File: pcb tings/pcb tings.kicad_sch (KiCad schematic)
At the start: 2 parts

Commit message: Finally back to working on this
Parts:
- added C?: 1uF, symbol Device:C_Small
- added R? (x2): 22, symbol Device:R_Small
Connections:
- net GND: now also C?.2
- net at U?.3 (D-): now also R?.2
- net at U?.4 (D+): now also R?.2
- net at U?.6 (UCAP): now also C?.1
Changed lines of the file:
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@@
   (junction (at 55.88 50.8) (diameter 0) (color 0 0 0 0)
   )
+  (wire (pts (xy 35.56 83.82) (xy 43.18 83.82))
+    (stroke (width 0) (type default) (color 0 0 0 0))
+  )
+  (wire (pts (xy 29.21 86.36) (xy 43.18 86.36))
+    (stroke (width 0) (type default) (color 0 0 0 0))
+  )
+  (wire (pts (xy 20.32 83.82) (xy 30.48 83.82))
+    (stroke (width 0) (type default) (color 0 0 0 0))
+  )
+  (wire (pts (xy 20.32 86.36) (xy 24.13 86.36))
+    (stroke (width 0) (type default) (color 0 0 0 0))
+  )
   (wire (pts (xy 73.66 111.76) (xy 90.17 111.76))
     (stroke (width 0) (type default) (color 0 0 0 0))
@@
     (stroke (width 0) (type default) (color 0 0 0 0))
   )
+  (wire (pts (xy 29.21 91.44) (xy 43.18 91.44))
+    (stroke (width 0) (type default) (color 0 0 0 0))
+  )
   (wire (pts (xy 58.42 50.8) (xy 60.96 50.8))
+    (stroke (width 0) (type default) (color 0 0 0 0))
+  )
+  (wire (pts (xy 29.21 96.52) (xy 29.21 99.06))
     (stroke (width 0) (type default) (color 0 0 0 0))
   )
@@
     (pin "1")
   )
+  (symbol (lib_id "Device:R_Small") (at 26.67 86.36 90) (unit 1)
+    (in_bom yes) (on_board yes)
+    (property "Reference" "R?" (id 0) (at 26.67 81.28 90))
+    (property "Value" "22" (id 1) (at 26.67 83.82 90))
+    (property "Footprint" "" (id 2) (at 26.67 86.36 0)
+      (effects (font (size 1.27 1.27)) hide)
+    )
+    (property "Datasheet" "~" (id 3) (at 26.67 86.36 0)
+      (effects (font (size 1.27 1.27)) hide)
+    )
+    (pin "1")
+    (pin "2")
+  )
   (symbol (lib_id "power:+5V") (at 55.88 44.45 0) (unit 1)
     (in_bom yes) (on_board yes) (fields_autoplaced)
@@
     (pin "1")
   )
+  (symbol (lib_id "power:GND") (at 29.21 99.06 0) (unit 1)
+    (in_bom yes) (on_board yes) (fields_autoplaced)
+    (property "Reference" "#PWR?" (id 0) (at 29.21 105.41 0)
+      (effects (font (size 1.27 1.27)) hide)
+    )
+    (property "Value" "GND" (id 1) (at 29.21 104.14 0))
+    (property "Footprint" "" (id 2) (at 29.21 99.06 0)
+      (effects (font (size 1.27 1.27)) hide)
+    )
+    (property "Datasheet" "" (id 3) (at 29.21 99.06 0)
+      (effects (font (size 1.27 1.27)) hide)
+    )
+    (pin "1")
+  )
+  (symbol (lib_id "Device:R_Small") (at 33.02 83.82 90) (unit 1)
+    (in_bom yes) (on_board yes)
+    (property "Reference" "R?" (id 0) (at 34.29 78.74 90)
+      (effects (font (size 1.27 1.27)) (justify left))
+    )
+    (property "Value" "22" (id 1) (at 34.29 81.28 90)
+      (effects (font (size 1.27 1.27)) (justify left))
+    )
+    (property "Footprint" "" (id 2) (at 33.02 83.82 0)
+      (effects (font (size 1.27 1.27)) hide)
+    )
+    (property "Datasheet" "~" (id 3) (at 33.02 83.82 0)
+      (effects (font (size 1.27 1.27)) hide)
+    )
+    (pin "1")
+    (pin "2")
+  )
   (symbol (lib_id "MCU_Microchip_ATmega:ATmega32U4-A") (at 58.42 96.52 0) (unit 1)
-    (in_bom yes) (on_board yes) (fields_autoplaced)
-    (property "Reference" "U?" (id 0) (at 60.4394 142.24 0)
-      (effects (font (size 1.27 1.27)) (justify left))
-    )
-    (property "Value" "ATmega32U4-A" (id 1) (at 60.4394 144.78 0)
+    (in_bom yes) (on_board yes)
+    (property "Reference" "U?" (id 0) (at 59.69 143.51 0)
+      (effects (font (size 1.27 1.27)) (justify left))
+    )
+    (property "Value" "ATmega32U4-A" (id 1) (at 53.34 146.05 0)
       (effects (font (size 1.27 1.27)) (justify left))
     )
@@
   )
   (symbol (lib_id "power:GND") (at 48.26 142.24 0) (unit 1)
-    (in_bom yes) (on_board yes) (fields_autoplaced)
+    (in_bom yes) (on_board yes)
     (property "Reference" "#PWR?" (id 0) (at 48.26 148.59 0)
       (effects (font (size 1.27 1.27)) hide)
     )
-    (property "Value" "GND" (id 1) (at 48.26 147.32 0))
+    (property "Value" "GND" (id 1) (at 48.26 146.05 0))
     (property "Footprint" "" (id 2) (at 48.26 142.24 0)
       (effects (font (size 1.27 1.27)) hide)
@@
     (pin "2")
   )
+  (symbol (lib_id "Device:C_Small") (at 29.21 93.98 0) (unit 1)
+    (in_bom yes) (on_board yes) (fields_autoplaced)
+    (property "Reference" "C?" (id 0) (at 31.75 92.7162 0)
+      (effects (font (size 1.27 1.27)) (justify left))
+    )
+    (property "Value" "1uF" (id 1) (at 31.75 95.2562 0)
+      (effects (font (size 1.27 1.27)) (justify left))
+    )
+    (property "Footprint" "" (id 2) (at 29.21 93.98 0)
+      (effects (font (size 1.27 1.27)) hide)
+    )
+    (property "Datasheet" "~" (id 3) (at 29.21 93.98 0)
+      (effects (font (size 1.27 1.27)) hide)
+    )
+    (pin "1")
+    (pin "2")
+  )
   (sheet_instances
     (path "/" (page "1"))
@@
       (reference "#PWR?") (unit 1) (value "+5V") (footprint "")
     )
+    (path "/afa30aab-dcdf-4492-b0da-da07511df226"
+      (reference "#PWR?") (unit 1) (value "GND") (footprint "")
+    )
     (path "/b6b05379-33d6-4201-bb25-f13b46745b60"
       (reference "#PWR?") (unit 1) (value "GND") (footprint "")
     )
+    (path "/d5f3ae9d-63b3-4045-bc16-4f0d0bf26073"
+      (reference "C?") (unit 1) (value "1uF") (footprint "")
+    )
+    (path "/7c2e75b3-ed26-4254-b6d2-b338f546c2e5"
+      (reference "R?") (unit 1) (value "22") (footprint "")
+    )
+    (path "/b07e4fa3-ea3e-4f85-8ece-bb79c07ff759"
+      (reference "R?") (unit 1) (value "22") (footprint "")
+    )
     (path "/ca5557ee-df94-426c-a0ce-8db8275385ae"

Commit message: completed MCU zone
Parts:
- added C? (x2): 22pF, symbol Device:C_Small
- added C? (x3): 0.1uF, symbol Device:C_Small
- added C?: 10uF, symbol Device:C_Small
- added R?: 10k, symbol Device:R_Small
- added SW?: SW_Push, symbol Switch:SW_Push
- added Y?: 16MHz, symbol Device:Crystal_GND24_Small
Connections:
- net +5V: now also U?.7 (VBUS), C?.1, C?.1, C?.1, C?.1, R?.1
- net GND: now also C?.1, C?.1, C?.2, C?.2, C?.2, C?.2, SW?.1, Y?.2, Y?.4
- net at U?.13 (~{RESET}): now also R?.2, SW?.2
- net at U?.16 (XTAL2): now also C?.2, Y?.3
- net at U?.17 (XTAL1): now also C?.2, Y?.1
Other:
- moved on the sheet: C?, R?, U?

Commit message: power
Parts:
- added D? (x4): SOD-123, symbol Device:D_Small
- added F?: 500mA, symbol Device:Polyfuse
- added MX? (x4): MX-NoLED, symbol MX_Alps_Hybrid:MX-NoLED
- added USB?: Molex-0548190589, symbol random-keyboard-parts:Molex-0548190589
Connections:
- net +5V: now also F?.2
- net D+: now also USB?.3 (D+)
- net D-: now also USB?.4 (D-)
- net GND: now also USB?.1 (GND)
- new net: D?.2 (A), MX?.2 (ROW) (x4)
- new net: D?.1 (K), D?.1 (K) (x2)
- new net COL0: MX?.1 (COL), MX?.1 (COL)
- new net COL1: MX?.1 (COL), MX?.1 (COL)
- new net VCC: F?.1, USB?.5 (VBUS)

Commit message: finished assigning foot prints
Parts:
- C1, C2, C3, C4, C5, C6, C7: renamed from C?; footprint (none) -> Capacitor_SMD:C_0805_2012Metric
- D1, D2, D3, D4: renamed from D?; footprint (none) -> Diode_SMD:D_SOD-123
- F1: renamed from F?; footprint (none) -> Fuse:Fuse_1206_3216Metric
- MX1, MX2, MX3, MX4: renamed from MX?; footprint (none) -> MX_Alps_Hybrid:MX-1U-NoLED
- R1, R2, R3, R4: renamed from R?; footprint (none) -> Resistor_SMD:R_0805_2012Metric
- SW1: renamed from SW?; footprint (none) -> random-keyboard-parts:SKQG-1155865
- USB1: renamed from USB?; footprint (none) -> random-keyboard-parts:Molex-0548190589
- Y1: renamed from Y?; footprint (none) -> Crystal:Crystal_SMD_3225-4Pin_3.2x2.5mm
- gave numbers to parts that had none: 1

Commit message: creating pcb
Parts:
- renumbered D3 to D2, D2 to D3
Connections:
- net COL0: now also MX3.1 (COL); no longer MX2.1 (COL)
- net COL1: now also MX2.1 (COL); no longer MX3.1 (COL)
- net at D2.2 (A): now also MX2.2 (ROW); no longer MX3.2 (ROW)
- net at D3.2 (A): now also MX3.2 (ROW); no longer MX2.2 (ROW)
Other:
- moved on the sheet: MX2, MX3
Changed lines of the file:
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@@
   (junction (at 129.54 48.26) (diameter 0) (color 0 0 0 0)
   )
+  (junction (at 243.84 93.98) (diameter 0) (color 0 0 0 0)
+  )
   (junction (at 110.49 55.88) (diameter 0) (color 0 0 0 0)
   )
@@
   (junction (at 81.28 119.38) (diameter 0) (color 0 0 0 0)
   )
-  (junction (at 243.84 93.98) (diameter 0) (color 0 0 0 0)
-  )
   (junction (at 76.2 119.38) (diameter 0) (color 0 0 0 0)
   )
@@
     (stroke (width 0) (type default) (color 0 0 0 0))
   )
+  (wire (pts (xy 243.84 93.98) (xy 243.84 110.49))
+    (stroke (width 0) (type default) (color 0 0 0 0))
+  )
   (wire (pts (xy 67.31 124.46) (xy 76.2 124.46))
     (stroke (width 0) (type default) (color 0 0 0 0))
@@
   )
   (wire (pts (xy 127 139.7) (xy 119.38 139.7))
-    (stroke (width 0) (type default) (color 0 0 0 0))
-  )
-  (wire (pts (xy 243.84 93.98) (xy 243.84 110.49))
     (stroke (width 0) (type default) (color 0 0 0 0))
   )
@@
   (symbol (lib_id "Device:D_Small") (at 234.95 101.6 90) (unit 1)
     (in_bom yes) (on_board yes)
-    (property "Reference" "D3" (id 0) (at 232.41 102.87 0)
+    (property "Reference" "D2" (id 0) (at 232.41 102.87 0)
       (effects (font (size 1 1)) (justify left))
     )
@@
     (pin "2")
   )
+  (symbol (lib_id "MX_Alps_Hybrid:MX-NoLED") (at 240.03 95.25 0) (unit 1)
+    (in_bom yes) (on_board yes)
+    (property "Reference" "MX2" (id 0) (at 240.03 90.17 0)
+      (effects (font (size 1.524 1.524)))
+    )
+    (property "Value" "MX-NoLED" (id 1) (at 240.03 91.44 0)
+      (effects (font (size 0.508 0.508)))
+    )
+    (property "Footprint" "MX_Alps_Hybrid:MX-1U-NoLED" (id 2) (at 224.155 95.885 0)
+      (effects (font (size 1.524 1.524)) hide)
+    )
+    (property "Datasheet" "" (id 3) (at 224.155 95.885 0)
+      (effects (font (size 1.524 1.524)) hide)
+    )
+    (pin "1")
+    (pin "2")
+  )
+  (symbol (lib_id "power:+5V") (at 127 41.91 0) (unit 1)
+    (in_bom yes) (on_board yes) (fields_autoplaced)
+    (property "Reference" "#PWR0104" (id 0) (at 127 45.72 0)
+      (effects (font (size 1.27 1.27)) hide)
+    )
+    (property "Value" "+5V" (id 1) (at 127 36.83 0))
+    (property "Footprint" "" (id 2) (at 127 41.91 0)
+      (effects (font (size 1.27 1.27)) hide)
+    )
+    (property "Datasheet" "" (id 3) (at 127 41.91 0)
+      (effects (font (size 1.27 1.27)) hide)
+    )
+    (pin "1")
+  )
+  (symbol (lib_id "Device:D_Small") (at 234.95 118.11 90) (unit 1)
+    (in_bom yes) (on_board yes)
+    (property "Reference" "D4" (id 0) (at 232.41 119.38 0)
+      (effects (font (size 1 1)) (justify left))
+    )
+    (property "Value" "SOD-123" (id 1) (at 232.41 116.84 0)
+      (effects (font (size 1 1)) (justify left))
+    )
+    (property "Footprint" "Diode_SMD:D_SOD-123" (id 2) (at 234.95 118.11 90)
+      (effects (font (size 1.27 1.27)) hide)
+    )
+    (property "Datasheet" "~" (id 3) (at 234.95 118.11 90)
+      (effects (font (size 1.27 1.27)) hide)
+    )
+    (pin "1")
+    (pin "2")
+  )
+  (symbol (lib_id "power:+5V") (at 81.28 116.84 0) (unit 1)
+    (in_bom yes) (on_board yes) (fields_autoplaced)
+    (property "Reference" "#PWR0113" (id 0) (at 81.28 120.65 0)
+      (effects (font (size 1.27 1.27)) hide)
+    )
+    (property "Value" "+5V" (id 1) (at 81.28 111.76 0))
+    (property "Footprint" "" (id 2) (at 81.28 116.84 0)
+      (effects (font (size 1.27 1.27)) hide)
+    )
+    (property "Datasheet" "" (id 3) (at 81.28 116.84 0)
+      (effects (font (size 1.27 1.27)) hide)
+    )
+    (pin "1")
+  )
+  (symbol (lib_id "power:GND") (at 91.44 53.34 0) (unit 1)
+    (in_bom yes) (on_board yes) (fields_autoplaced)
+    (property "Reference" "#PWR0102" (id 0) (at 91.44 59.69 0)
+      (effects (font (size 1.27 1.27)) hide)
+    )
+    (property "Value" "GND" (id 1) (at 91.44 58.42 0))
+    (property "Footprint" "" (id 2) (at 91.44 53.34 0)
+      (effects (font (size 1.27 1.27)) hide)
+    )
+    (property "Datasheet" "" (id 3) (at 91.44 53.34 0)
+      (effects (font (size 1.27 1.27)) hide)
+    )
+    (pin "1")
+  )
   (symbol (lib_id "MX_Alps_Hybrid:MX-NoLED") (at 223.52 111.76 0) (unit 1)
     (in_bom yes) (on_board yes)
-    (property "Reference" "MX2" (id 0) (at 223.52 106.68 0)
+    (property "Reference" "MX3" (id 0) (at 223.52 106.68 0)
       (effects (font (size 1.524 1.524)))
     )
@@
     )
     (property "Datasheet" "" (id 3) (at 207.645 112.395 0)
-      (effects (font (size 1.524 1.524)) hide)
-    )
-    (pin "1")
-    (pin "2")
-  )
-  (symbol (lib_id "power:+5V") (at 127 41.91 0) (unit 1)
-    (in_bom yes) (on_board yes) (fields_autoplaced)
-    (property "Reference" "#PWR0104" (id 0) (at 127 45.72 0)
-      (effects (font (size 1.27 1.27)) hide)
-    )
-    (property "Value" "+5V" (id 1) (at 127 36.83 0))
-    (property "Footprint" "" (id 2) (at 127 41.91 0)
-      (effects (font (size 1.27 1.27)) hide)
-    )
-    (property "Datasheet" "" (id 3) (at 127 41.91 0)
-      (effects (font (size 1.27 1.27)) hide)
-    )
-    (pin "1")
-  )
-  (symbol (lib_id "Device:D_Small") (at 234.95 118.11 90) (unit 1)
-    (in_bom yes) (on_board yes)
-    (property "Reference" "D4" (id 0) (at 232.41 119.38 0)
-      (effects (font (size 1 1)) (justify left))
-    )
-    (property "Value" "SOD-123" (id 1) (at 232.41 116.84 0)
-      (effects (font (size 1 1)) (justify left))
-    )
-    (property "Footprint" "Diode_SMD:D_SOD-123" (id 2) (at 234.95 118.11 90)
-      (effects (font (size 1.27 1.27)) hide)
-    )
-    (property "Datasheet" "~" (id 3) (at 234.95 118.11 90)
-      (effects (font (size 1.27 1.27)) hide)
-    )
-    (pin "1")
-    (pin "2")
-  )
-  (symbol (lib_id "power:+5V") (at 81.28 116.84 0) (unit 1)
-    (in_bom yes) (on_board yes) (fields_autoplaced)
-    (property "Reference" "#PWR0113" (id 0) (at 81.28 120.65 0)
-      (effects (font (size 1.27 1.27)) hide)
-    )
-    (property "Value" "+5V" (id 1) (at 81.28 111.76 0))
-    (property "Footprint" "" (id 2) (at 81.28 116.84 0)
-      (effects (font (size 1.27 1.27)) hide)
-    )
-    (property "Datasheet" "" (id 3) (at 81.28 116.84 0)
-      (effects (font (size 1.27 1.27)) hide)
-    )
-    (pin "1")
-  )
-  (symbol (lib_id "power:GND") (at 91.44 53.34 0) (unit 1)
-    (in_bom yes) (on_board yes) (fields_autoplaced)
-    (property "Reference" "#PWR0102" (id 0) (at 91.44 59.69 0)
-      (effects (font (size 1.27 1.27)) hide)
-    )
-    (property "Value" "GND" (id 1) (at 91.44 58.42 0))
-    (property "Footprint" "" (id 2) (at 91.44 53.34 0)
-      (effects (font (size 1.27 1.27)) hide)
-    )
-    (property "Datasheet" "" (id 3) (at 91.44 53.34 0)
-      (effects (font (size 1.27 1.27)) hide)
-    )
-    (pin "1")
-  )
-  (symbol (lib_id "MX_Alps_Hybrid:MX-NoLED") (at 240.03 95.25 0) (unit 1)
-    (in_bom yes) (on_board yes)
-    (property "Reference" "MX3" (id 0) (at 240.03 90.17 0)
-      (effects (font (size 1.524 1.524)))
-    )
-    (property "Value" "MX-NoLED" (id 1) (at 240.03 91.44 0)
-      (effects (font (size 0.508 0.508)))
-    )
-    (property "Footprint" "MX_Alps_Hybrid:MX-1U-NoLED" (id 2) (at 224.155 95.885 0)
-      (effects (font (size 1.524 1.524)) hide)
-    )
-    (property "Datasheet" "" (id 3) (at 224.155 95.885 0)
       (effects (font (size 1.524 1.524)) hide)
     )
@@
   (symbol (lib_id "Device:D_Small") (at 218.44 118.11 90) (unit 1)
     (in_bom yes) (on_board yes)
-    (property "Reference" "D2" (id 0) (at 215.9 119.38 0)
+    (property "Reference" "D3" (id 0) (at 215.9 119.38 0)
       (effects (font (size 1 1)) (justify left))
     )
@@
       (reference "D1") (unit 1) (value "SOD-123") (footprint "Diode_SMD:D_SOD-123")
     )
+    (path "/6e952d51-1d1e-42c9-9266-945473b5cf2f"
+      (reference "D2") (unit 1) (value "SOD-123") (footprint "Diode_SMD:D_SOD-123")
+    )
     (path "/e66c77c3-e1d8-4bcc-a6bf-fa400b066ed7"
-      (reference "D2") (unit 1) (value "SOD-123") (footprint "Diode_SMD:D_SOD-123")
-    )
-    (path "/6e952d51-1d1e-42c9-9266-945473b5cf2f"
       (reference "D3") (unit 1) (value "SOD-123") (footprint "Diode_SMD:D_SOD-123")
     )

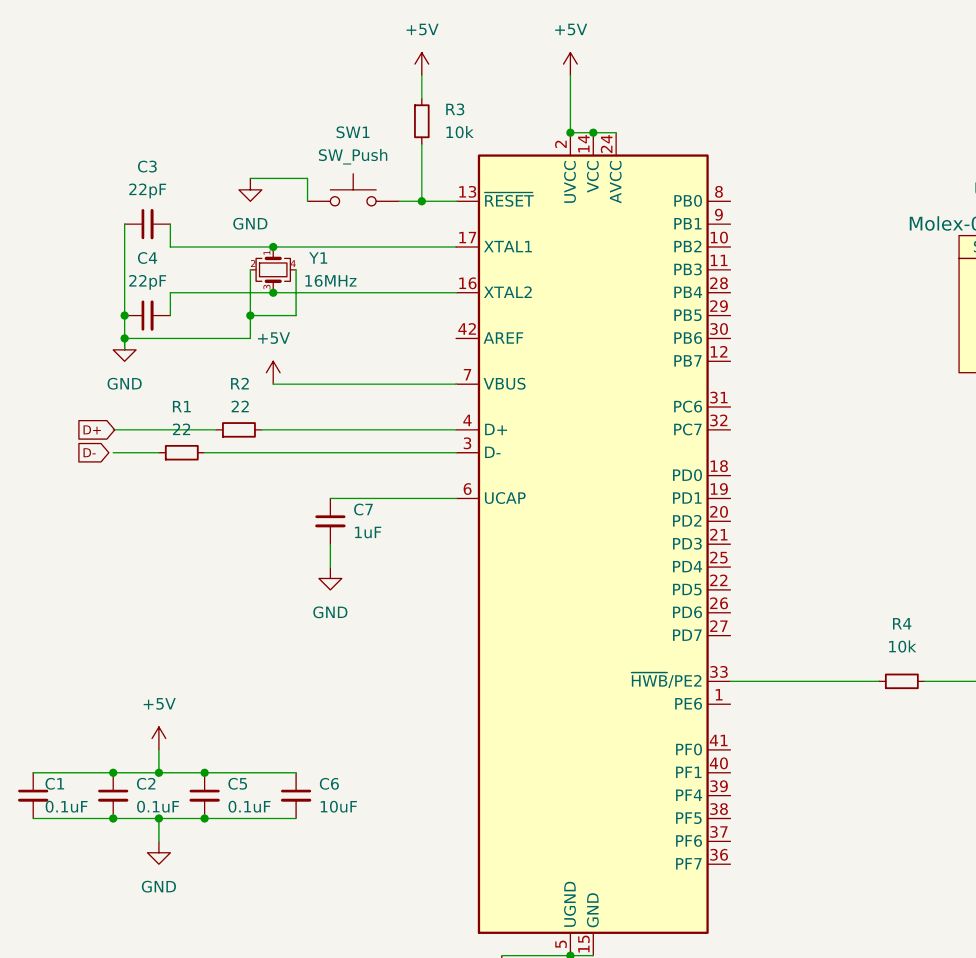
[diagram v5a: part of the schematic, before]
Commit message: Fixed footprints and edgecuts
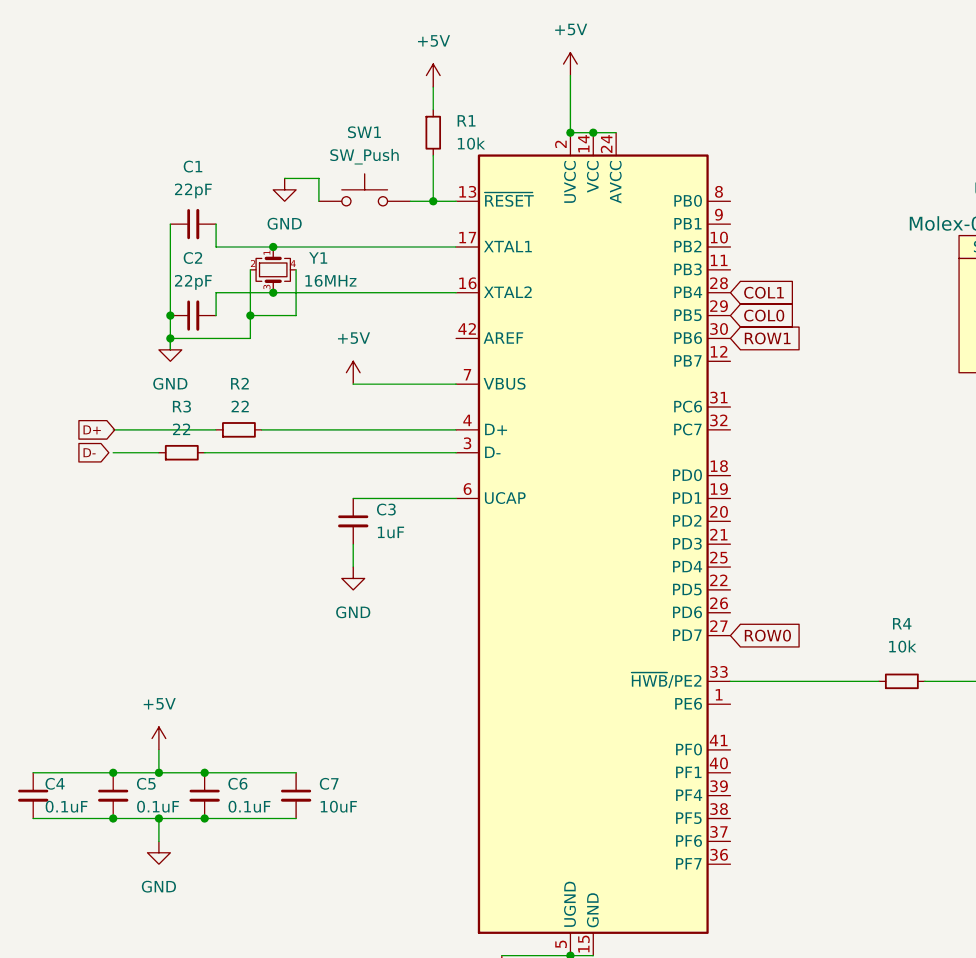
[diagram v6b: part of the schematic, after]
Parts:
- renumbered C3 to C1, C4 to C2, C7 to C3, C1 to C4, C2 to C5, C5 to C6, C6 to C7, R3 to R1, R1 to R3
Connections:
- net COL0: now also U1.29 (PB5)
- net COL1: now also U1.28 (PB4)
- net ROW0: now also U1.27 (PD7)
- net ROW1: now also U1.30 (PB6)
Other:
- moved on the sheet: C1, C2, C3, R1, SW1
